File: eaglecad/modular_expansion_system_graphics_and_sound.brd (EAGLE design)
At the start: 90.2 x 100 mm, 44 parts, among them IC1 74LS244N, IC8 74LS244N, IC9-74HCU04 74LS04N, J1-WAIT-AND-INT WAIT-AND-INT, J1_ADDRESS_CON j1, J2_DATA_AND_POWER_CON j2, J3-VIDEO-OUT RCA, J4-AUDIO-LEFT RCA, J5-AUDIO-RIGHT RCA, Q2 2N2222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

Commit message: small change to game board
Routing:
- net TMS9918_AD6-TMS4416_A1: track 62.8 -> 63.9 mm
- net D1: track 147.0 -> 146.1 mm
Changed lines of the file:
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@@
 <wire x1="37.875" y1="90.625" x2="37.805" y2="90.535" width="0.3" layer="1"/>
 <wire x1="52" y1="97.75" x2="52.07" y2="97.79" width="0.3" layer="1"/>
-<wire x1="60.625" y1="31" x2="64.25" y2="27.375" width="0.3" layer="1"/>
-<wire x1="60.625" y1="31" x2="60.625" y2="33.5" width="0.3" layer="1"/>
+<wire x1="61.25" y1="30.375" x2="64.25" y2="27.375" width="0.3" layer="1"/>
+<wire x1="61.25" y1="30.375" x2="61.25" y2="32.875" width="0.3" layer="1"/>
 <wire x1="64.25" y1="27.375" x2="64.3325" y2="27.37" width="0.3" layer="1"/>
 <wire x1="43.625" y1="72.875" x2="41.625" y2="74.875" width="0.3" layer="1"/>
@@
 <wire x1="37.875" y1="90.5" x2="37.805" y2="90.535" width="0.3" layer="16"/>
 <wire x1="41.5" y1="75" x2="41.5075" y2="74.91" width="0.3" layer="16"/>
-<wire x1="60.625" y1="33.5" x2="58.8125" y2="35.3125" width="0.3" layer="1"/>
+<wire x1="61.25" y1="32.875" x2="58.8125" y2="35.3125" width="0.3" layer="1"/>
 <wire x1="58.8125" y1="35.3125" x2="57.1875" y2="35.3125" width="0.3" layer="1"/>
 <wire x1="54.3475" y1="39.0175" x2="55" y2="38.365" width="0.3" layer="1"/>
@@
 <wire x1="64.875" y1="97.75" x2="64.77" y2="97.79" width="0.3" layer="16"/>
 <wire x1="33.375" y1="65.25" x2="31.375" y2="67.25" width="0.3" layer="1"/>
-<wire x1="51.875" y1="65.25" x2="33.375" y2="65.25" width="0.3" layer="1"/>
-<wire x1="52.875" y1="66.25" x2="51.875" y2="65.25" width="0.3" layer="1"/>
-<wire x1="53.375" y1="66.25" x2="52.875" y2="66.25" width="0.3" layer="1"/>
-<wire x1="54.5" y1="65.125" x2="53.375" y2="66.25" width="0.3" layer="1"/>
-<wire x1="54.5" y1="63.75" x2="54.5" y2="65.125" width="0.3" layer="1"/>
+<wire x1="33.375" y1="65.25" x2="52.5" y2="65.25" width="0.3" layer="1"/>
+<wire x1="54.03125" y1="64.96875" x2="53.40625" y2="65.59375" width="0.3" layer="1"/>
 <wire x1="61.625" y1="63.75" x2="59.375" y2="63.75" width="0.3" layer="1"/>
 <wire x1="59.375" y1="63.75" x2="54.5" y2="63.75" width="0.3" layer="1"/>
@@
 <wire x1="59.75" y1="52.625" x2="59.0774" y2="53.2976" width="0.3" layer="16"/>
 <wire x1="59.0774" y1="53.2976" x2="59.0774" y2="62.2024" width="0.3" layer="16"/>
+<wire x1="52.5" y1="65.25" x2="52.84375" y2="65.59375" width="0.3" layer="1"/>
+<wire x1="52.84375" y1="65.59375" x2="53.40625" y2="65.59375" width="0.3" layer="1"/>
+<wire x1="54.5" y1="63.75" x2="54.03125" y2="64.21875" width="0.3" layer="1"/>
+<wire x1="54.03125" y1="64.21875" x2="54.03125" y2="64.96875" width="0.3" layer="1"/>
 </signal>
 <signal name="D4">
@@
 <contactref element="U1" pad="13"/>
 <contactref element="U3" pad="13"/>
-<wire x1="22.75" y1="27.75" x2="18.875" y2="23.875" width="0.3" layer="16"/>
-<wire x1="22.75" y1="56.875" x2="22.75" y2="27.75" width="0.3" layer="16"/>
-<wire x1="18.625" y1="61" x2="22.65625" y2="56.96875" width="0.3" layer="16"/>
+<wire x1="18.875" y1="23.875" x2="22.75" y2="27.75" width="0.3" layer="16"/>
 <wire x1="18.625" y1="61.25" x2="18.625" y2="61" width="0.3" layer="16"/>
 <wire x1="18.875" y1="23.875" x2="18.7875" y2="23.7775" width="0.3" layer="16"/>
@@
 <wire x1="41.75" y1="58.5" x2="43.25" y2="57" width="0.3" layer="1"/>
 <wire x1="30.3125" y1="58.5" x2="41.75" y2="58.5" width="0.3" layer="1"/>
-<wire x1="22.65625" y1="56.96875" x2="23.875" y2="58.1875" width="0.3" layer="16"/>
 <wire x1="43.25" y1="57" x2="43.2625" y2="56.945" width="0.3" layer="1"/>
 <via x="23.875" y="58.1875" extent="1-16" drill="0.35"/>
@@
 <wire x1="29.9375" y1="58.125" x2="30.3125" y2="58.5" width="0.3" layer="1"/>
 <wire x1="23.9375" y1="58.125" x2="29.9375" y2="58.125" width="0.3" layer="1"/>
-<wire x1="22.75" y1="56.875" x2="22.65625" y2="56.96875" width="0" layer="19" extent="16-16"/>
+<wire x1="18.5075" y1="61.3175" x2="21.6375" y2="58.1875" width="0.3" layer="16"/>
+<wire x1="21.6375" y1="58.1875" x2="23.875" y2="58.1875" width="0.3" layer="16"/>
+<wire x1="22.75" y1="27.75" x2="22.75" y2="47.875" width="0.3" layer="16"/>
+<wire x1="22.75" y1="47.875" x2="21.5625" y2="49.0625" width="0.3" layer="16"/>
+<wire x1="21.5625" y1="49.0625" x2="21.5625" y2="58.1125" width="0.3" layer="16"/>
+<wire x1="21.5625" y1="58.1125" x2="21.6375" y2="58.1875" width="0.3" layer="16"/>
 </signal>
 <signal name="TMS9918_AD5-TMS4416_A2">
@@
 <wire x1="24.75" y1="35.875" x2="24.0625" y2="36.5625" width="0.3" layer="16"/>
 <via x="24.0625" y="36.5625" extent="1-16" drill="0.35"/>
-<wire x1="23.5" y1="41.8125" x2="23.75" y2="41.5625" width="0.3" layer="16"/>
-<wire x1="23.5" y1="56" x2="23.5" y2="41.8125" width="0.3" layer="16"/>
+<wire x1="23.8125" y1="49" x2="23.75" y2="48.9375" width="0.3" layer="16"/>
+<wire x1="23.75" y1="48.9375" x2="23.75" y2="41.5625" width="0.3" layer="16"/>
+<wire x1="23.5" y1="56" x2="23.8125" y2="55.6875" width="0.3" layer="16"/>
+<wire x1="23.8125" y1="55.6875" x2="23.8125" y2="49" width="0.3" layer="16"/>
 <via x="23.75" y="41.5625" extent="1-16" drill="0.35"/>
 <wire x1="23.75" y1="41.5625" x2="23.75" y2="40.47713125" width="0.3" layer="1"/>
@@
 <wire x1="15.375" y1="54.75" x2="15" y2="54.75" width="0.3" layer="1"/>
 <wire x1="18.75" y1="51.375" x2="15.375" y2="54.75" width="0.3" layer="1"/>
-<wire x1="41" y1="51.375" x2="18.75" y2="51.375" width="0.3" layer="1"/>
-<wire x1="43" y1="49.375" x2="41" y2="51.375" width="0.3" layer="1"/>
+<wire x1="20" y1="51.375" x2="18.75" y2="51.375" width="0.3" layer="1"/>
 <wire x1="43.25" y1="49.375" x2="43" y2="49.375" width="0.3" layer="1"/>
 <wire x1="11" y1="61.25" x2="10.8875" y2="61.3175" width="0.3" layer="1"/>
@@
 <via x="37.625" y="42.875" extent="1-16" drill="0.35"/>
 <via x="43.0625" y="46.5" extent="1-16" drill="0.35"/>
+<wire x1="20.5" y1="51.875" x2="20" y2="51.375" width="0.3" layer="1"/>
+<wire x1="43" y1="49.375" x2="40.5" y2="51.875" width="0.3" layer="1"/>
+<wire x1="40.5" y1="51.875" x2="20.5" y2="51.875" width="0.3" layer="1"/>
 </signal>
 <signal name="TMS9918_AD0-TMS4416_A7">
@@
 <contactref element="RN1" pad="5"/>
 <contactref element="JOYSTICK2" pad="4"/>
-<wire x1="65.875" y1="69.25" x2="64.25" y2="67.625" width="0.3" layer="1"/>
-<wire x1="72.25" y1="69.25" x2="65.875" y2="69.25" width="0.3" layer="1"/>
-<wire x1="73.125" y1="70.125" x2="72.25" y2="69.25" width="0.3" layer="1"/>
+<wire x1="65.5625" y1="68.9375" x2="64.25" y2="67.625" width="0.3" layer="1"/>
+<wire x1="71.9375" y1="68.9375" x2="65.5625" y2="68.9375" width="0.3" layer="1"/>
+<wire x1="73.125" y1="70.125" x2="71.9375" y2="68.9375" width="0.3" layer="1"/>
 <wire x1="74.125" y1="70.125" x2="73.125" y2="70.125" width="0.3" layer="1"/>
 <wire x1="64.25" y1="67.625" x2="64.14" y2="67.5375" width="0.3" layer="1"/>
@@
 <wire x1="55.125" y1="58.75" x2="57.625" y2="58.75" width="0.3" layer="1"/>
 <wire x1="53.125" y1="60.75" x2="55.125" y2="58.75" width="0.3" layer="1"/>
-<wire x1="53.125" y1="65.5" x2="53.125" y2="60.75" width="0.3" layer="1"/>
-<wire x1="50.125" y1="68.5" x2="53.125" y2="65.5" width="0.3" layer="16"/>
-<wire x1="50.125" y1="79.5" x2="50.125" y2="68.5" width="0.3" layer="16"/>
+<wire x1="53.125" y1="64.875" x2="53.125" y2="60.75" width="0.3" layer="1"/>
+<wire x1="53.125" y1="64.875" x2="50.125" y2="67.875" width="0.3" layer="16"/>
+<wire x1="50.125" y1="79.5" x2="50.125" y2="67.875" width="0.3" layer="16"/>
 <wire x1="67.5" y1="44" x2="67.4175" y2="43.88" width="0.3" layer="1"/>
 <wire x1="50.125" y1="79.5" x2="50.165" y2="79.525" width="0.3" layer="16"/>
-<via x="53.125" y="65.5" extent="1-16" drill="0.35"/>
+<via x="53.125" y="64.875" extent="1-16" drill="0.35"/>
 </signal>
 <signal name="WR*">

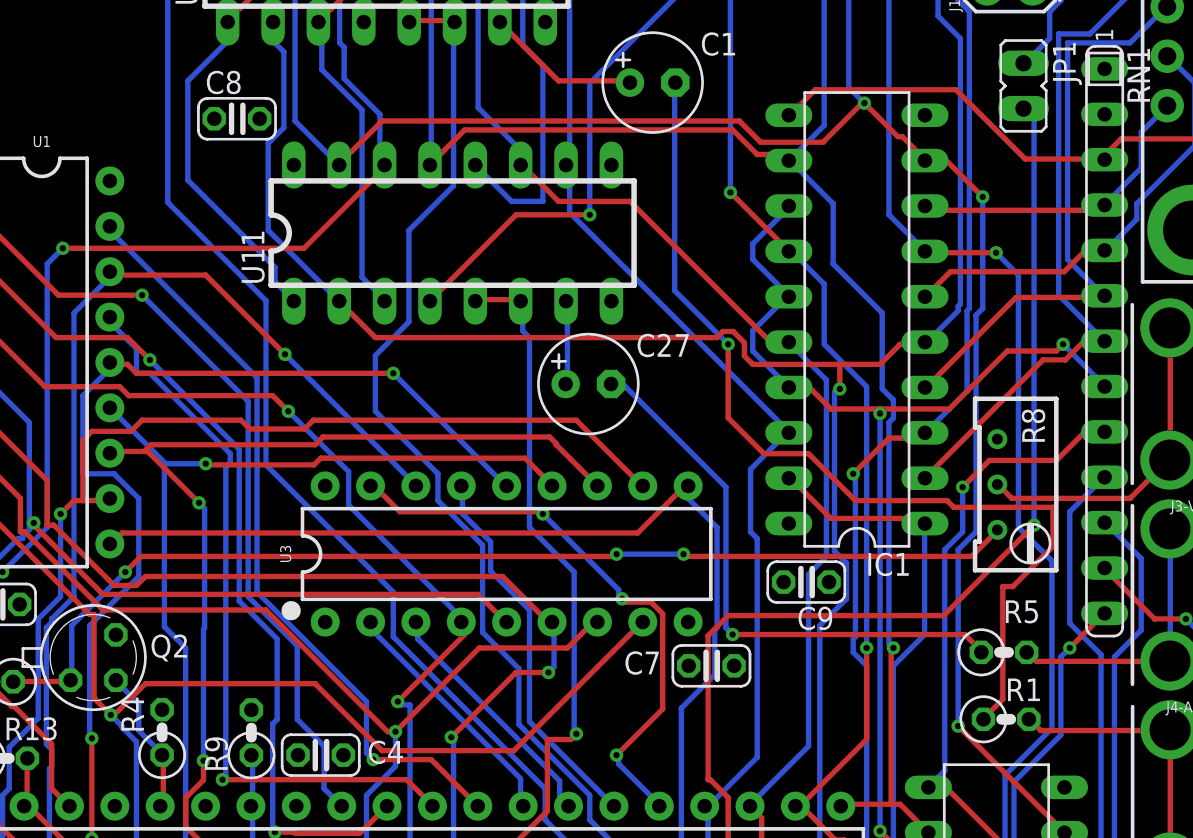
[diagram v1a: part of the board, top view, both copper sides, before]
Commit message: cleaned up wire stub
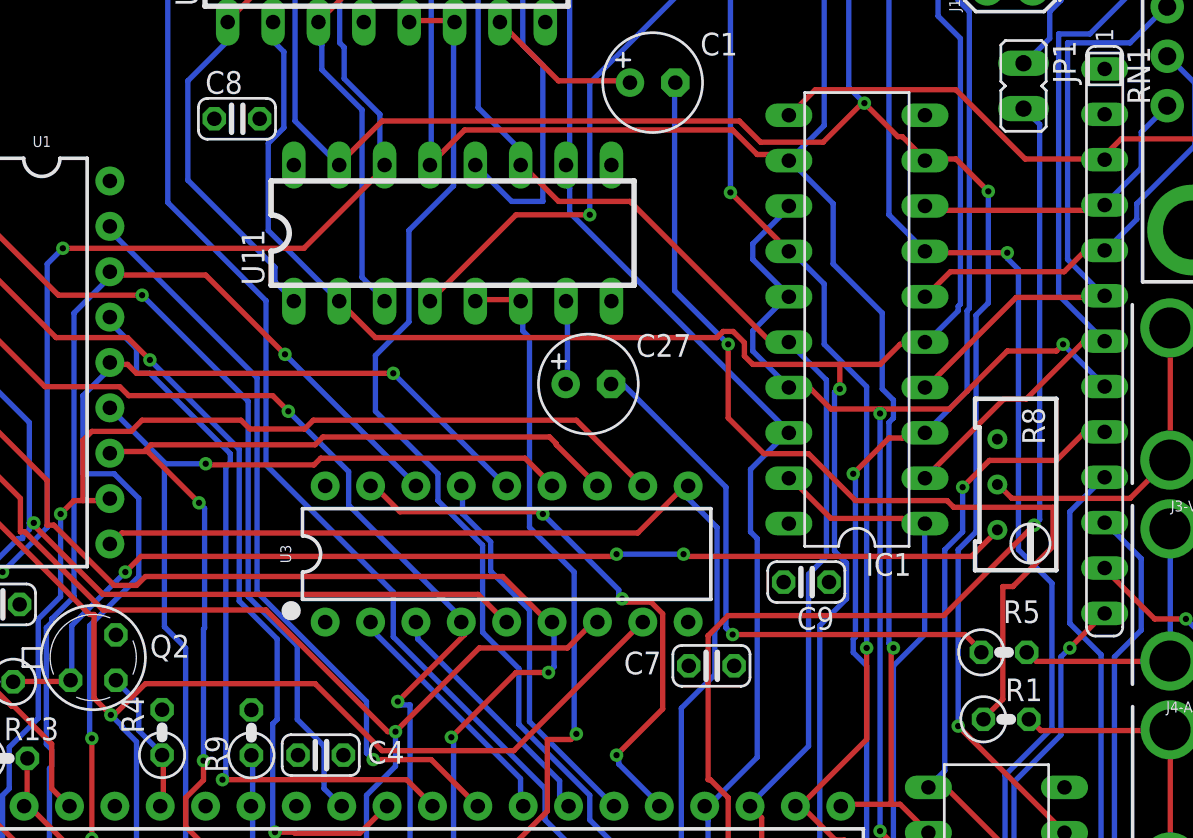
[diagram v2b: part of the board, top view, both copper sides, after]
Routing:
- net D3: track 140.7 -> 141.4 mm
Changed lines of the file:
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@@
 <wire x1="68.625" y1="40.75" x2="68.625" y2="29.25" width="0.3" layer="16"/>
 <wire x1="71.25" y1="43.375" x2="68.625" y2="40.75" width="0.3" layer="16"/>
-<wire x1="71.25" y1="52.75" x2="71.25" y2="43.375" width="0.3" layer="16"/>
-<wire x1="69.375" y1="54.625" x2="71.25" y2="52.75" width="0.3" layer="16"/>
-<wire x1="69.375" y1="68.75" x2="69.375" y2="54.625" width="0.3" layer="16"/>
-<wire x1="68.125" y1="70" x2="69.375" y2="68.75" width="0.3" layer="16"/>
-<wire x1="64.25" y1="70" x2="68.125" y2="70" width="0.3" layer="1"/>
+<wire x1="71.25" y1="51.5" x2="71.25" y2="43.375" width="0.3" layer="16"/>
+<wire x1="69.375" y1="53.375" x2="71.25" y2="51.5" width="0.3" layer="16"/>
+<wire x1="69.375" y1="69.0625" x2="69.375" y2="53.375" width="0.3" layer="16"/>
+<wire x1="69.375" y1="69.0625" x2="68.75" y2="69.6875" width="0.3" layer="16"/>
+<wire x1="68.75" y1="70" x2="68.75" y2="69.6875" width="0.3" layer="16"/>
+<wire x1="64.25" y1="70" x2="68.75" y2="70" width="0.3" layer="1"/>
 <wire x1="67.125" y1="27.75" x2="67.125" y2="27.625" width="0.3" layer="16"/>
 <wire x1="64.25" y1="70" x2="64.14" y2="70.0775" width="0.3" layer="1"/>
 <via x="67.125" y="27.625" extent="1-16" drill="0.35"/>
-<via x="68.125" y="70" extent="1-16" drill="0.35"/>
+<via x="68.75" y="70" extent="1-16" drill="0.35"/>
 </signal>
 <signal name="D5">
@@
 <wire x1="67" y1="54.375" x2="66" y2="53.375" width="0.3" layer="16"/>
 <wire x1="67" y1="66.5" x2="67" y2="54.375" width="0.3" layer="16"/>
-<wire x1="67.375" y1="66.875" x2="67" y2="66.5" width="0.3" layer="16"/>
-<wire x1="67.375" y1="73.125" x2="67.375" y2="66.875" width="0.3" layer="16"/>
-<wire x1="65.25" y1="75.25" x2="67.375" y2="73.125" width="0.3" layer="1"/>
-<wire x1="64.25" y1="75.25" x2="65.25" y2="75.25" width="0.3" layer="1"/>
+<wire x1="67.6875" y1="67.1875" x2="67" y2="66.5" width="0.3" layer="16"/>
+<wire x1="67.6875" y1="73.4375" x2="67.6875" y2="67.1875" width="0.3" layer="16"/>
+<wire x1="65.875" y1="75.25" x2="67.6875" y2="73.4375" width="0.3" layer="1"/>
+<wire x1="64.25" y1="75.25" x2="65.875" y2="75.25" width="0.3" layer="1"/>
 <wire x1="71.875" y1="37.625" x2="71.9525" y2="37.53" width="0.3" layer="1"/>
 <wire x1="64.25" y1="75.25" x2="64.14" y2="75.1575" width="0.3" layer="1"/>
@@
 <via x="60.75" y="78.375" extent="1-16" drill="0.35"/>
 <via x="66" y="43.5" extent="1-16" drill="0.35"/>
-<via x="67.375" y="73.125" extent="1-16" drill="0.35"/>
+<via x="67.6875" y="73.4375" extent="1-16" drill="0.35"/>
 </signal>
 <signal name="SN76489-CLOCK">
@@
 <contactref element="U3" pad="13"/>
 <wire x1="18.875" y1="23.875" x2="22.75" y2="27.75" width="0.3" layer="16"/>
-<wire x1="18.625" y1="61.25" x2="18.625" y2="61" width="0.3" layer="16"/>
 <wire x1="18.875" y1="23.875" x2="18.7875" y2="23.7775" width="0.3" layer="16"/>
-<wire x1="18.625" y1="61.25" x2="18.5075" y2="61.3175" width="0.3" layer="16"/>
 <wire x1="41.75" y1="58.5" x2="43.25" y2="57" width="0.3" layer="1"/>
 <wire x1="30.3125" y1="58.5" x2="41.75" y2="58.5" width="0.3" layer="1"/>
@@
 <contactref element="RN1" pad="7"/>
 <contactref element="JOYSTICK2" pad="2"/>
-<wire x1="70.75" y1="64" x2="64.25" y2="57.5" width="0.3" layer="1"/>
-<wire x1="72" y1="64" x2="70.75" y2="64" width="0.3" layer="1"/>
-<wire x1="73" y1="65" x2="72" y2="64" width="0.3" layer="1"/>
+<wire x1="68.5625" y1="61.8125" x2="64.25" y2="57.5" width="0.3" layer="1"/>
+<wire x1="69.8125" y1="61.8125" x2="68.5625" y2="61.8125" width="0.3" layer="1"/>
+<wire x1="73" y1="65" x2="69.8125" y2="61.8125" width="0.3" layer="1"/>
 <wire x1="74.125" y1="65" x2="73" y2="65" width="0.3" layer="1"/>
 <wire x1="64.25" y1="57.5" x2="64.14" y2="57.3775" width="0.3" layer="1"/>
@@
 <contactref element="U2" pad="P16"/>
 <contactref element="JP1" pad="2"/>
-<wire x1="70.25" y1="77.5" x2="69.75" y2="78" width="0.3" layer="16"/>
-<wire x1="70.25" y1="54.75" x2="70.25" y2="77.5" width="0.3" layer="16"/>
+<wire x1="70.5625" y1="77.1875" x2="69.75" y2="78" width="0.3" layer="16"/>
+<wire x1="70.5625" y1="77.1875" x2="70.5625" y2="55.0625" width="0.3" layer="16"/>
+<wire x1="70.25" y1="54.75" x2="70.5625" y2="55.0625" width="0.3" layer="16"/>
 <wire x1="65.1875" y1="49.6875" x2="70.25" y2="54.75" width="0.3" layer="1"/>
 <wire x1="53.125" y1="49.6875" x2="65.1875" y2="49.6875" width="0.3" layer="1"/>
